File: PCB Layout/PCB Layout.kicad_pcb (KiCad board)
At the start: 2 copper layers, 151.6 x 100.3 mm, 15 parts, among them J1 Conn_01x15, J2 Conn_01x15, J3 Screw_Terminal_01x04, J4 Conn_01x02

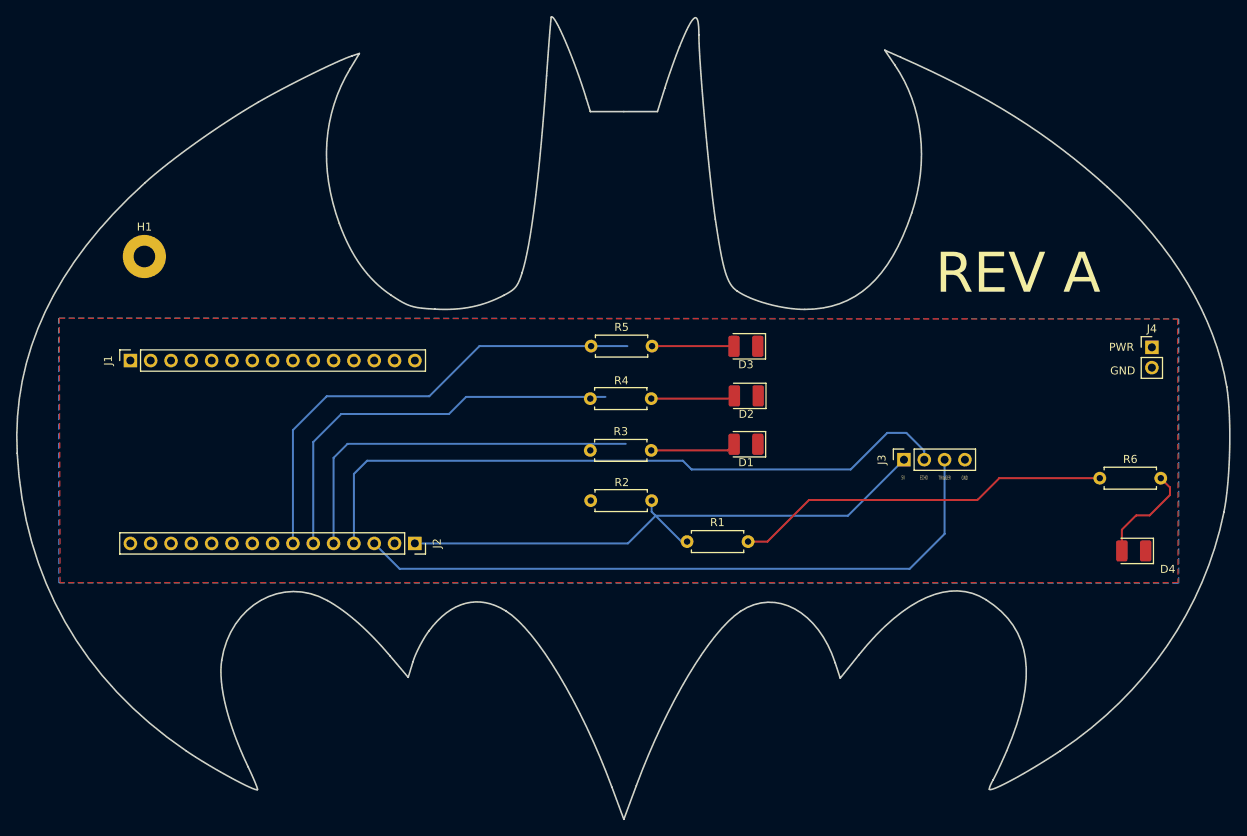
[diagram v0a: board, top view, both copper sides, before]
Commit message: This increased the esp32 footprint to be spaced by 26.25 mm
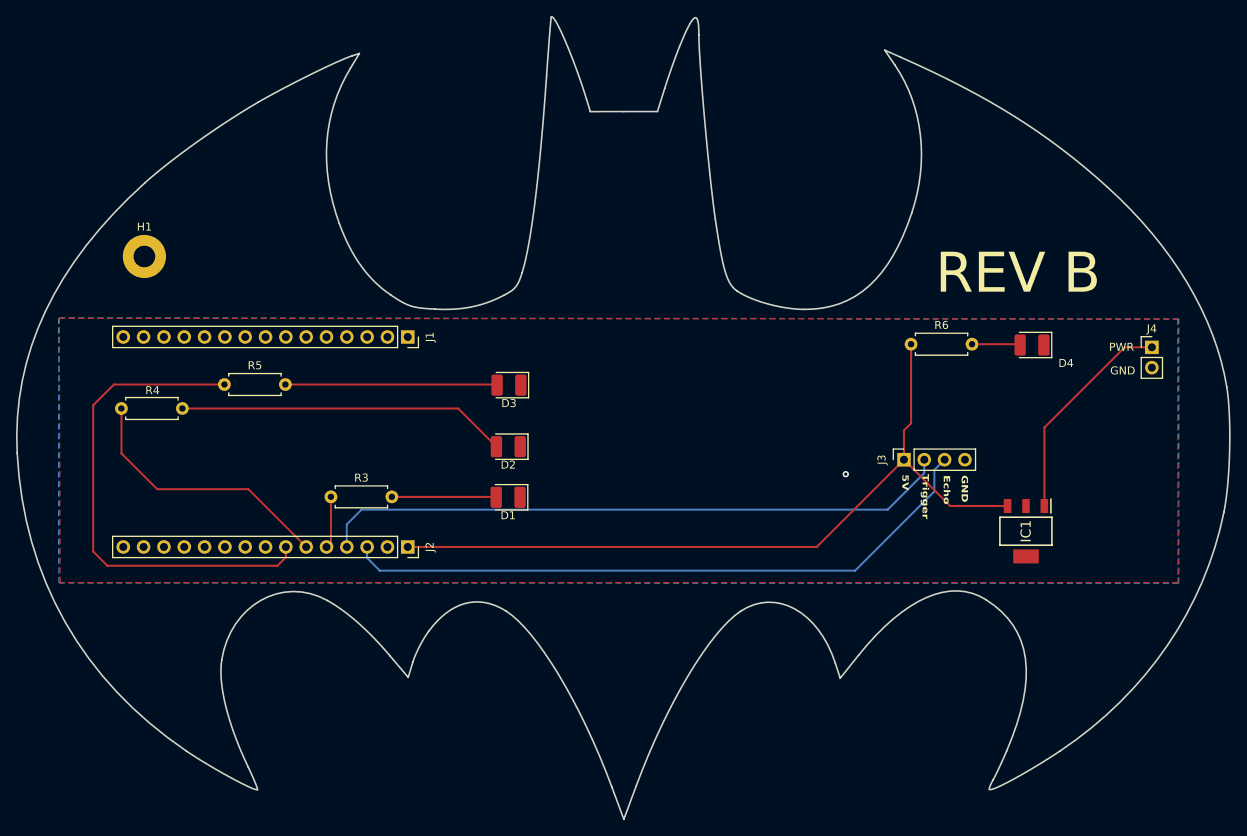
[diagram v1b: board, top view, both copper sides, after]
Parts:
- removed R1: 200, Resistor_THT:R_Axial_DIN0207_L6.3mm_D2.5mm_P7.62mm_Horizontal
- removed R2: 300, Resistor_THT:R_Axial_DIN0207_L6.3mm_D2.5mm_P7.62mm_Horizontal
- added IC1: LM340MP-5.0_NOPB, SamacSys:SOT230P700X180-4N, F.Cu at (207.3, 100.2)
- moved R4 58.6 mm to (101.8, 84.9)
- moved R5 46.1 mm to (107.1, 81.9)
- moved J1 34.8 mm to (130.0, 75.9), turned to -90 degrees
- moved R3 32.9 mm to (120.4, 95.9)
- moved D1 30.5 mm to (142.5, 96.0)
- moved D2 30.4 mm to (142.6, 89.7)
- moved D3 30.0 mm to (142.6, 82.0)
- moved R6 28.9 mm to (192.9, 76.8)
- moved D4 28.7 mm to (208.0, 77.0)
- moved J2 0.99 mm to (130.0, 102.2)
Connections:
- J2 pad 1: Net-(J2-Pin_1) -> Net-(IC1-OUTPUT)
- J3 pad 1: Net-(J2-Pin_1) -> Net-(IC1-OUTPUT)
- R6 pad 1: +9V -> Net-(IC1-OUTPUT)
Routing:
- net Net-(IC1-OUTPUT): track 0.00 -> 96.7 mm
- net Net-(J2-Pin_1): track 72.8 -> 0.00 mm
- net Net-(J2-Pin_5): track 47.9 -> 6.49 mm
- net Net-(D2-A): track 10.5 -> 41.2 mm
- net +9V: track 47.3 -> 27.4 mm
- net Net-(J2-Pin_6): track 51.5 -> 33.5 mm
- net Net-(D3-A): track 10.3 -> 26.5 mm
- net Net-(D4-A): track 13.4 -> 6.06 mm
- net Net-(J2-Pin_4): track 85.1 -> 79.1 mm
- net Net-(D1-A): track 10.7 -> 13.2 mm
- net Net-(J2-Pin_7): track 60.3 -> 62.3 mm
- net Net-(J2-Pin_3): track 83.7 -> 81.7 mm
- net GND: vias 0 -> 1
- added copper zone on B.Cu, net GND
- removed copper zone on B.Cu, net +9V
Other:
- board text added: "Echo"
- board text added: "REV B"
- board text added: "Trigger"
- board text removed: "ECHO"
- board text removed: "REV A"
- board text removed: "TRIGGER"
